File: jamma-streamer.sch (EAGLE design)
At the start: 18 parts, among them J1 Audio line out, J3 SDCARD, U1 LP298X, U3 74HC4050D

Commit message: Added atmega328p and begining wiring
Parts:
- removed C1: 0.1uF/16V, CMS:C1210C104K4J
- removed C2: 10uF/10V, CMS:C1210C106K8N
- removed U1: LP298X, LP2981-33DBVR:LP2981-33DBVRDBV5-M
- added C3, C6: 0.1uF/16V, CMS:KEMET-C1210C104K4J
- added C4: 10uF/10V, CMS:KEMET-C1210C106K8N
- added C5: 0.33uF/50V, CMS:KEMET-C1206X334K5R
- added IC1: LM7805, linear:7805DT
- added R2: 10Kohms, CMS:BOURNS-CRM2512AJW103ELF
- added U2: ATMEGA328PB-AUR, ATMEGA328PB-AUR:ATMEGA328PB-AUR
- added U4: LP298X, LP2981-33DBVR:LP2981-33DBVRDBV5-M
- R1: device CMS:652-CHP0603FX1001ELF -> CMS:BOURNS-652CHP0603FX1001ELF
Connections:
- net -5V renamed JAMMA-5V
- removed net +12V: JAMMA_IN.+12V@6, JAMMA_IN.+12V@F, JAMMA_OUT_BTM.+12V, JAMMA_OUT_TOP.+12V
- removed net +3.3V: C2.P$2, J3.VDD, U1.VOUT, U3.VCC
- removed net +5V: C1.P$2, JAMMA_IN.+5V@3, JAMMA_IN.+5V@4, JAMMA_IN.+5V@C, JAMMA_IN.+5V@D, JAMMA_OUT_BTM.+5V@1, JAMMA_OUT_BTM.+5V@2, JAMMA_OUT_TOP.+5V@1, JAMMA_OUT_TOP.+5V@2, U1.ON/!OFF, U1.VIN
- new net JAMMA+12V: C5.P$1, IC1.VI, JAMMA_IN.+12V@6, JAMMA_IN.+12V@F, JAMMA_OUT_BTM.+12V, JAMMA_OUT_TOP.+12V
- new net JAMMA+5V: JAMMA_IN.+5V@3, JAMMA_IN.+5V@4, JAMMA_IN.+5V@C, JAMMA_IN.+5V@D, JAMMA_OUT_BTM.+5V@1, JAMMA_OUT_BTM.+5V@2, JAMMA_OUT_TOP.+5V@1, JAMMA_OUT_TOP.+5V@2
- new net N$9: R2.P$2, U2.PC6/!RESET
- new net VCC: C3.P$2, C6.P$1, IC1.VO, R2.P$1, U2.VCC, U4.ON/!OFF, U4.VIN
- new net VCC_2: C4.P$2, J3.VDD, U3.VCC, U4.VOUT
- net GND: now also C3.P$1, C4.P$1, C5.P$2, C6.P$2, IC1.GND, U2.GND, U4.GND; no longer C1.P$1, C2.P$1, U1.GND

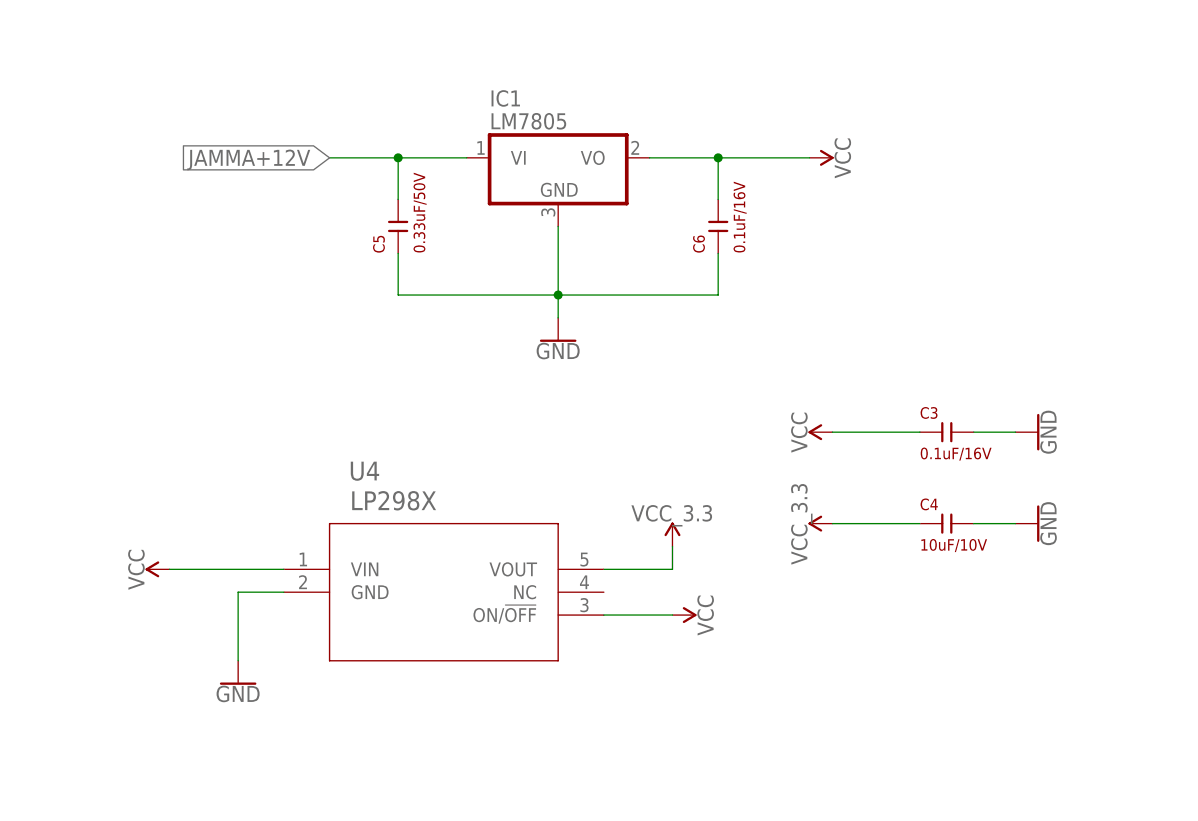
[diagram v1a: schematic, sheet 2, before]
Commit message: Schematic with atmega328p wired
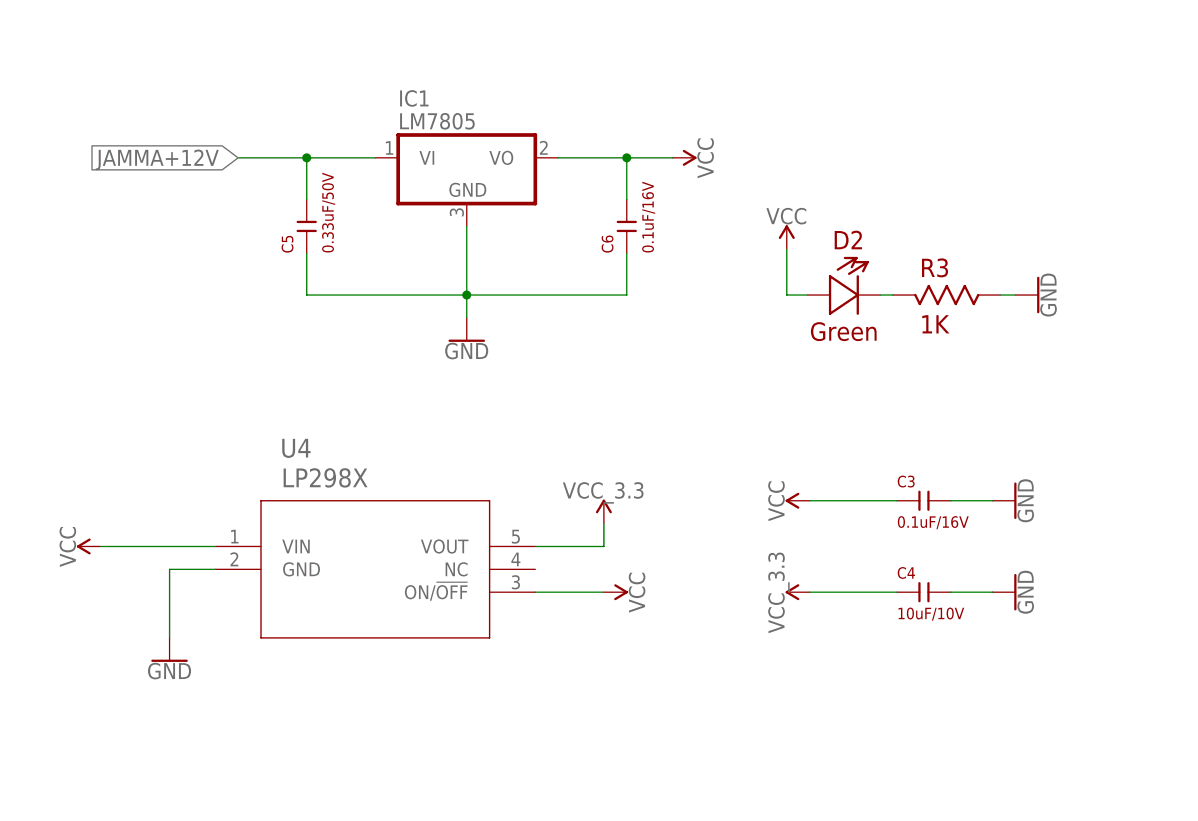
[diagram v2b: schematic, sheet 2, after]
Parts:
- added C1, C2: 22pF/25V, CMS:KEMET-C1206C334M5RAC
- added D2: Green, CMS:604-APTD1608LCGCK
- added J2: ICSP, SparkFun-Connectors:CONN_03X22X3_SILK_MALE_PTH
- added R3: 1K, CMS:BOURNS-652CHP0603FX1001ELF
- added S1: RESET SW, 1825910-7:1825910-7
- added Y1: 16MHz, SparkFun-Clocks:CRYSTAL-16MHZPTH-HC49US
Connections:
- removed net N$9: R2.P$2, U2.PC6/!RESET
- new net N$12: D2.P$2, R3.P$1
- new net N$13: C1.P$1, U2.PB6, Y1.2
- new net RESET: J2.5, R2.P$2, S1.3, S1.4, U2.PC6/!RESET
- net CLK: now also J2.3, U2.PD7
- net CS: now also C2.P$1, U2.PB7, Y1.1
- net DI: now also J2.4, U2.PD5
- net DO: now also J2.1, U2.PD6
- net GND: now also C1.P$2, C2.P$2, J2.6, R3.P$2, S1.1, S1.2; no longer U3.5Y, U3.6Y
- net VCC: now also D2.P$1, J2.2, U2.AVCC
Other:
- moved on the sheet: C3, C4, C5, C6, IC1, U4

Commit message: Adding button detection shift registers
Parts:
- added U1, U5, U6: CD74HC165MD16-M, CD74HC165M:CD74HC165MD16-M
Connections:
- removed net A: JAMMA_IN.2P-BTN2, JAMMA_OUT_BTM.2P6_PUSH2
- removed net B: JAMMA_IN.2P-BTN3, JAMMA_OUT_BTM.2P7_PUSH3
- removed net N$5: JAMMA_IN._D, JAMMA_OUT_BTM.2P9
- removed net N$6: JAMMA_IN._C, JAMMA_OUT_BTM.2P8
- removed net N$7: JAMMA_IN.25, JAMMA_OUT_TOP.1P8
- removed net N$8: JAMMA_IN.26, JAMMA_OUT_TOP.1P9
- new net 25: JAMMA_IN.25, JAMMA_OUT_TOP.1P8, U1.D1
- new net 26: JAMMA_IN.26, JAMMA_OUT_TOP.1P9, U1.D0
- new net N$10: U1.DS, U5.Q7
- new net N$9: U5.DS, U6.Q7
- new net PD4: U1.!PL, U2.PD4, U5.!PL, U6.!PL
- new net PD5: U1.!CE, U2.PD5, U5.!CE, U6.!CE
- new net PD6: U1.Q7, U2.PD6
- new net PD7: U1.CP, U2.PD7, U5.CP, U6.CP
- new net _A: JAMMA_IN.2P-BTN2, JAMMA_OUT_BTM.2P6_PUSH2, U1.D4
- new net _B: JAMMA_IN.2P-BTN3, JAMMA_OUT_BTM.2P7_PUSH3, U1.D5
- new net _C: JAMMA_IN._C, JAMMA_OUT_BTM.2P8, U1.D6
- new net _D: JAMMA_IN._D, JAMMA_OUT_BTM.2P9, U1.D7
- net 15: now also U6.D3
- net 16: now also U6.D2
- net 17: now also U6.D1
- net 18: now also U6.D0
- net 19: now also U5.D3
- net 20: now also U5.D2
- net 21: now also U5.D1
- net 22: now also U5.D0
- net 23: now also U1.D3
- net 24: now also U1.D2
- net CLK: now also U2.PB5; no longer U2.PD7
- net CS: now also U2.PB2
- net DI: now also U2.PB3; no longer U2.PD5
- net DO: now also U2.PB4; no longer U2.PD6
- net GND: now also U1.GND, U5.GND, U6.GND
- net R: now also U6.D4
- net T: now also U6.D5
- net U: now also U6.D6
- net V: now also U6.D7
- net VCC: now also U1.VCC, U5.VCC, U6.VCC
- net W: now also U5.D4
- net X: now also U5.D5
- net Y: now also U5.D6
- net Z: now also U5.D7
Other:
- note added: "Buttons detection PD4 = PLoad PD5 = Clock Enable PD6 = Data PD7 = Clock"
- note added: "Jamma is HIGH when not pressed (~3V) and LOW when pressed !"
- note added: "SD signals: CS = !SS0 (PB2) DI = MOSI0 (PB3) DO = MISO0 (PB4) CLK = SCK0 (PB5)"

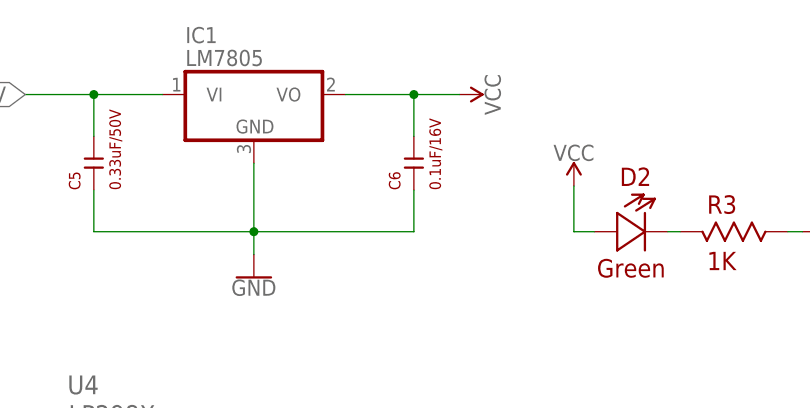
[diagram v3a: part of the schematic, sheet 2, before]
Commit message: Added FTDI USB to serial RS232
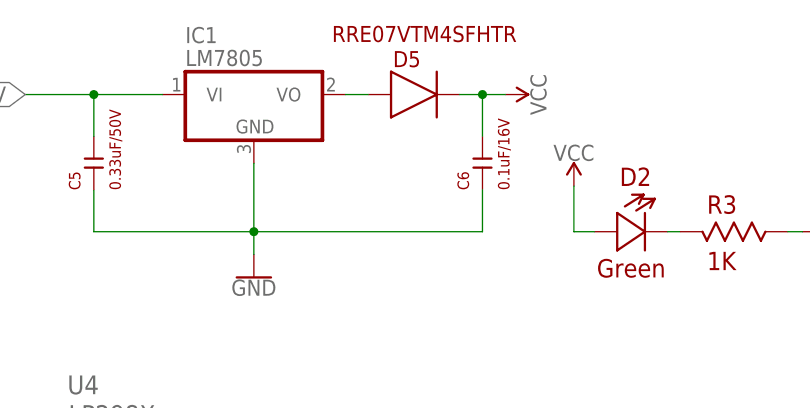
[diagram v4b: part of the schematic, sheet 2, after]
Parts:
- added C10: 10uF/10V, CMS:KEMET-C1210C106K8N
- added C7, C9: 0.1uF/16V, CMS:KEMET-C1210C104K4J
- added D3-RX, D4-TX: Green, CMS:604-APTD1608LCGCK
- added D5: RRE07VTM4SFHTR, RRE07VTM4SFHTR:RRE07VTM4SFHTR
- added F1: 6V/500mA, 1206L050YR:1206L050YRSMD
- added J4: 292304-1, 292304-1:292304-1
- added R4, R5: 1K, CMS:BOURNS-652CHP0603FX1001ELF
- added U7: FT232RL, SparkFun-IC-Comms:FT232RL-BASICSSOP
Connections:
- new net FTDI_RXD: U2.PD1, U7.RXD
- new net FTDI_TXD: U2.PD0, U7.TXD
- new net N$11: C7.P$2, U7.3V3OUT
- new net N$20: D4-TX.P$2, U7.TXLED
- new net N$21: D4-TX.P$1, R5.P$1
- new net N$22: D3-RX.P$1, R4.P$1
- new net N$23: D5.P$2, IC1.VO
- new net N$5: J4.D+, U7.USBDP
- new net N$6: J4.D-, U7.USBDM
- new net N$7: F1.P$1, J4.VBUS
- new net N$8: D3-RX.P$2, U7.RXLED
- new net VCCIO: R4.P$2, R5.P$2, U7.VCCIO
- net GND: now also C10.P$2, C7.P$1, C9.P$2, J4.GND, U7.AGND, U7.GND1, U7.GND2, U7.GND3, U7.TEST
- net VCC: now also C10.P$1, C9.P$1, D5.P$1, F1.P$2, U7.VCC; no longer IC1.VO
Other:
- moved on the sheet: C6

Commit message: final board v0.0.1
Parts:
- U4: value LP298X -> TLV757X / LP298X
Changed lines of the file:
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@@
 <part name="GND10" library="SparkFun-PowerSymbols" library_urn="urn:adsk.eagle:library:530" deviceset="GND" device=""/>
 <part name="SUPPLY1" library="SparkFun-PowerSymbols" library_urn="urn:adsk.eagle:library:530" deviceset="VCC" device=""/>
-<part name="U4" library="LP2981-33DBVR" deviceset="LP2981-33DBVR" device="DBV5-M" value="LP298X"/>
+<part name="U4" library="LP2981-33DBVR" deviceset="LP2981-33DBVR" device="DBV5-M" value="TLV757X / LP298X"/>
 <part name="GND11" library="SparkFun-PowerSymbols" library_urn="urn:adsk.eagle:library:530" deviceset="GND" device=""/>
 <part name="C3" library="CMS" deviceset="KEMET-C1210C104K4J" device="" value="0.1uF/16V"/>

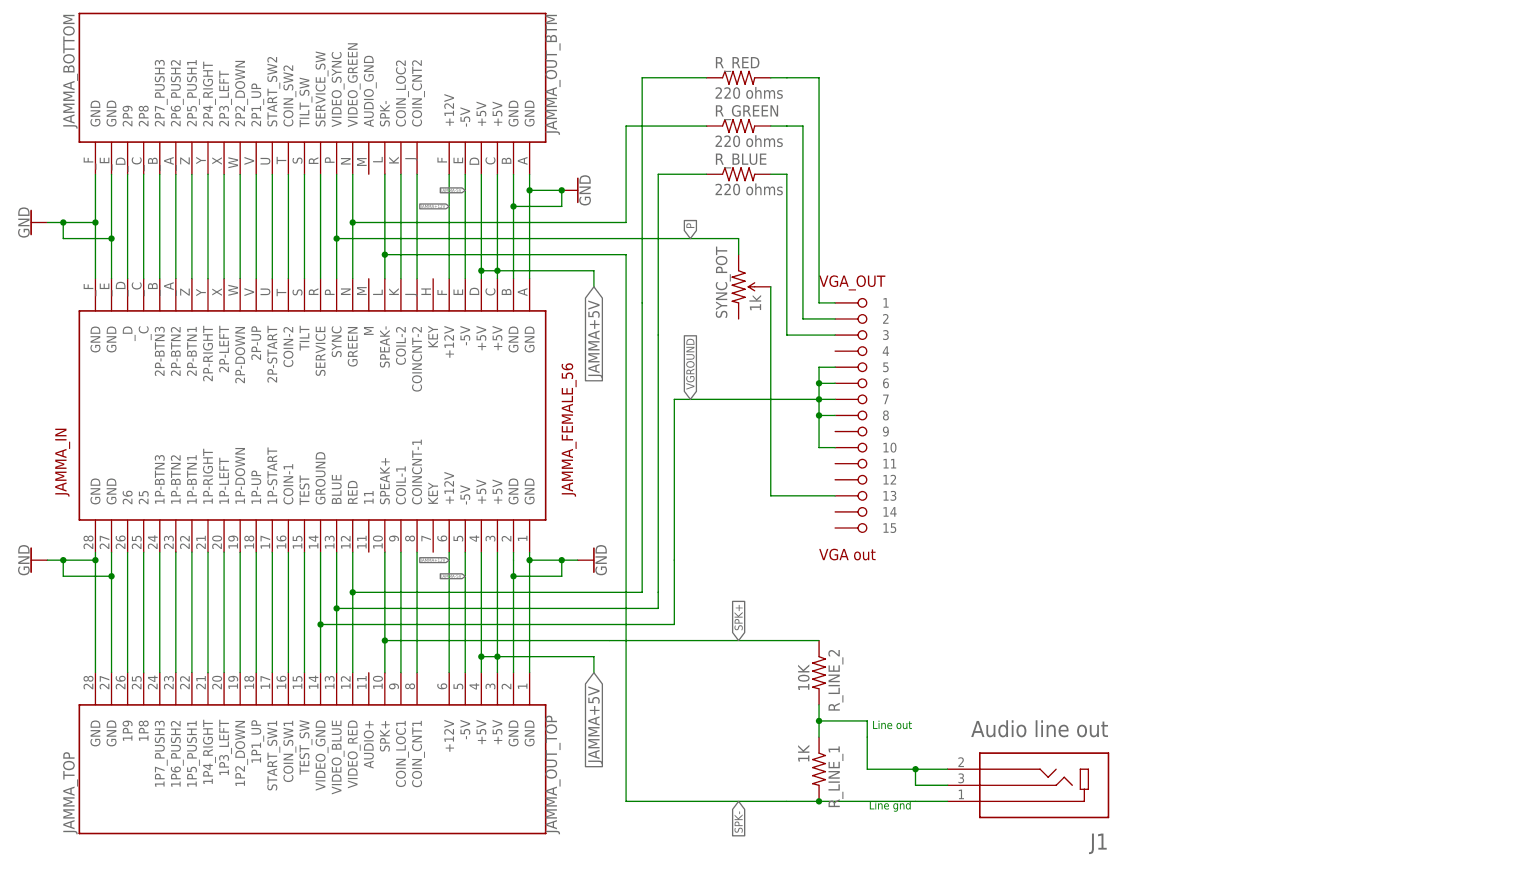
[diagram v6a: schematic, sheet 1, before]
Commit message: Better routes (unfinished) and audio circuit
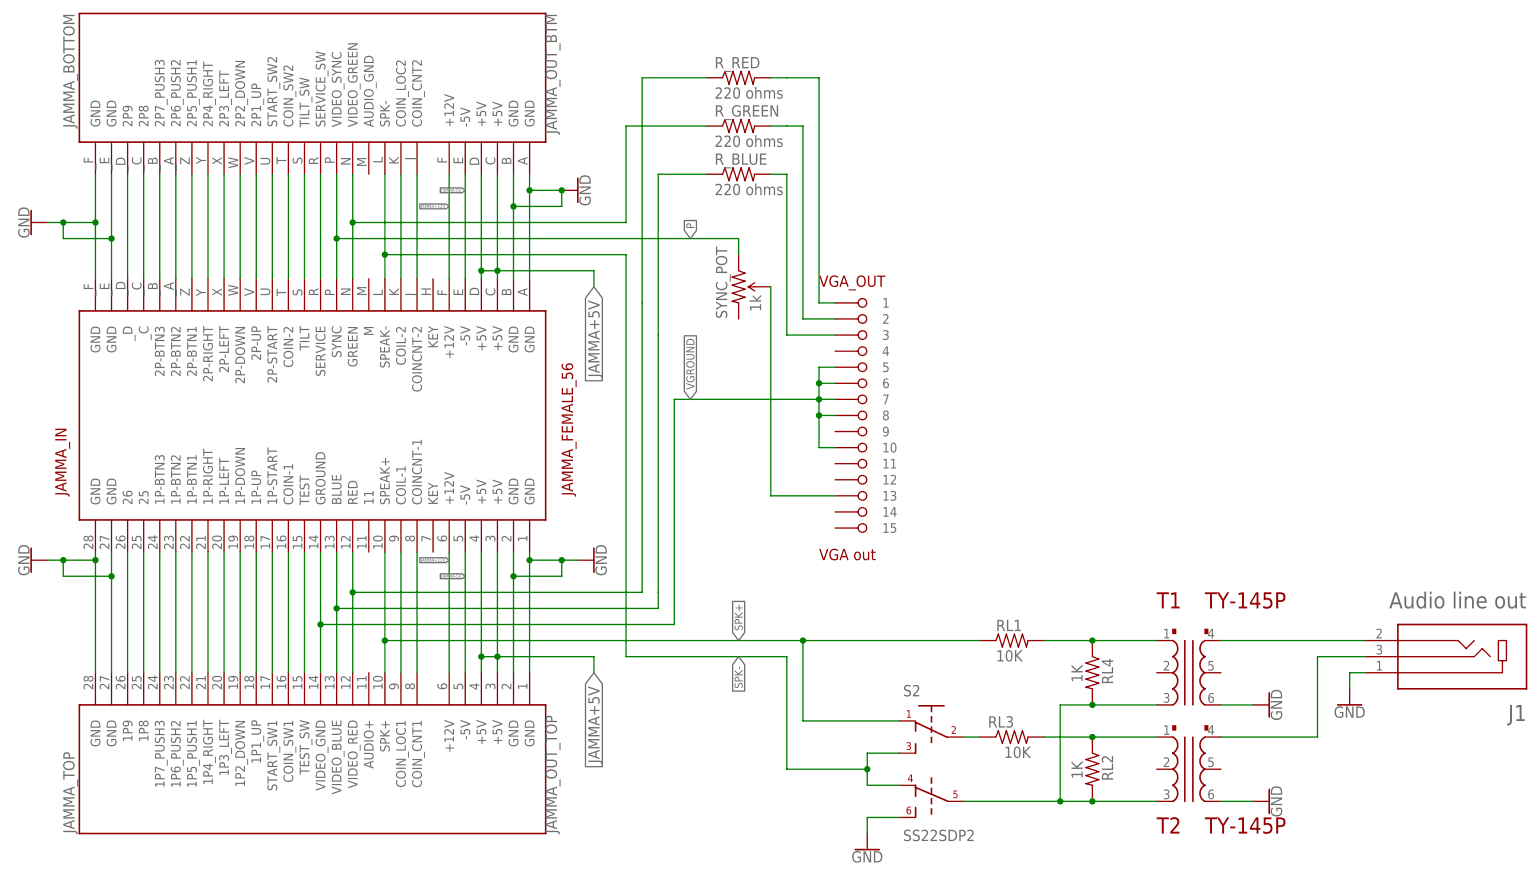
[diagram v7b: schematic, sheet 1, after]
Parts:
- removed R_LINE_1: 1K, rcl:R-US_0204/5
- removed R_LINE_2: 10K, rcl:R-US_0204/5
- added RL1, RL3: 10K, rcl:R-US_0204/5
- added RL2, RL4: 1K, rcl:R-US_0204/5
- added S2: SS22SDP2, SamacSys_Parts:SS22SDP2
- added T1, T2: TY-145P, TRIAD-TY-145P:TRIAD-TY-145P
- J4: value 292304-1 -> USB
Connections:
- new net N$24: RL1.2, RL4.1, T1.1
- new net N$25: RL2.2, RL4.2, S2.5, T1.3, T2.3
- new net N$26: J1.2, T1.4
- new net N$28: RL2.1, RL3.2, T2.1
- new net N$30: J1.3, T2.4
- net GND: now also J1.1, S2.6, T1.6, T2.6
- net N$4: now also RL3.1, S2.2; no longer J1.2, J1.3, R_LINE_1.1, R_LINE_2.2
- net SPK+: now also RL1.1, S2.1; no longer R_LINE_2.1
- net SPK-: now also S2.3, S2.4; no longer J1.1, R_LINE_1.2
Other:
- note removed: "Line gnd"
- note removed: "Line out"
- moved on the sheet: J1
